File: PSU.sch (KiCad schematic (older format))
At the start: 17 parts, among them P1 CONN_01X02, P2 CONN_01X01, P3 CONN_01X01, P4 CONN_01X01, Q1 BC817-40, U1 78L33

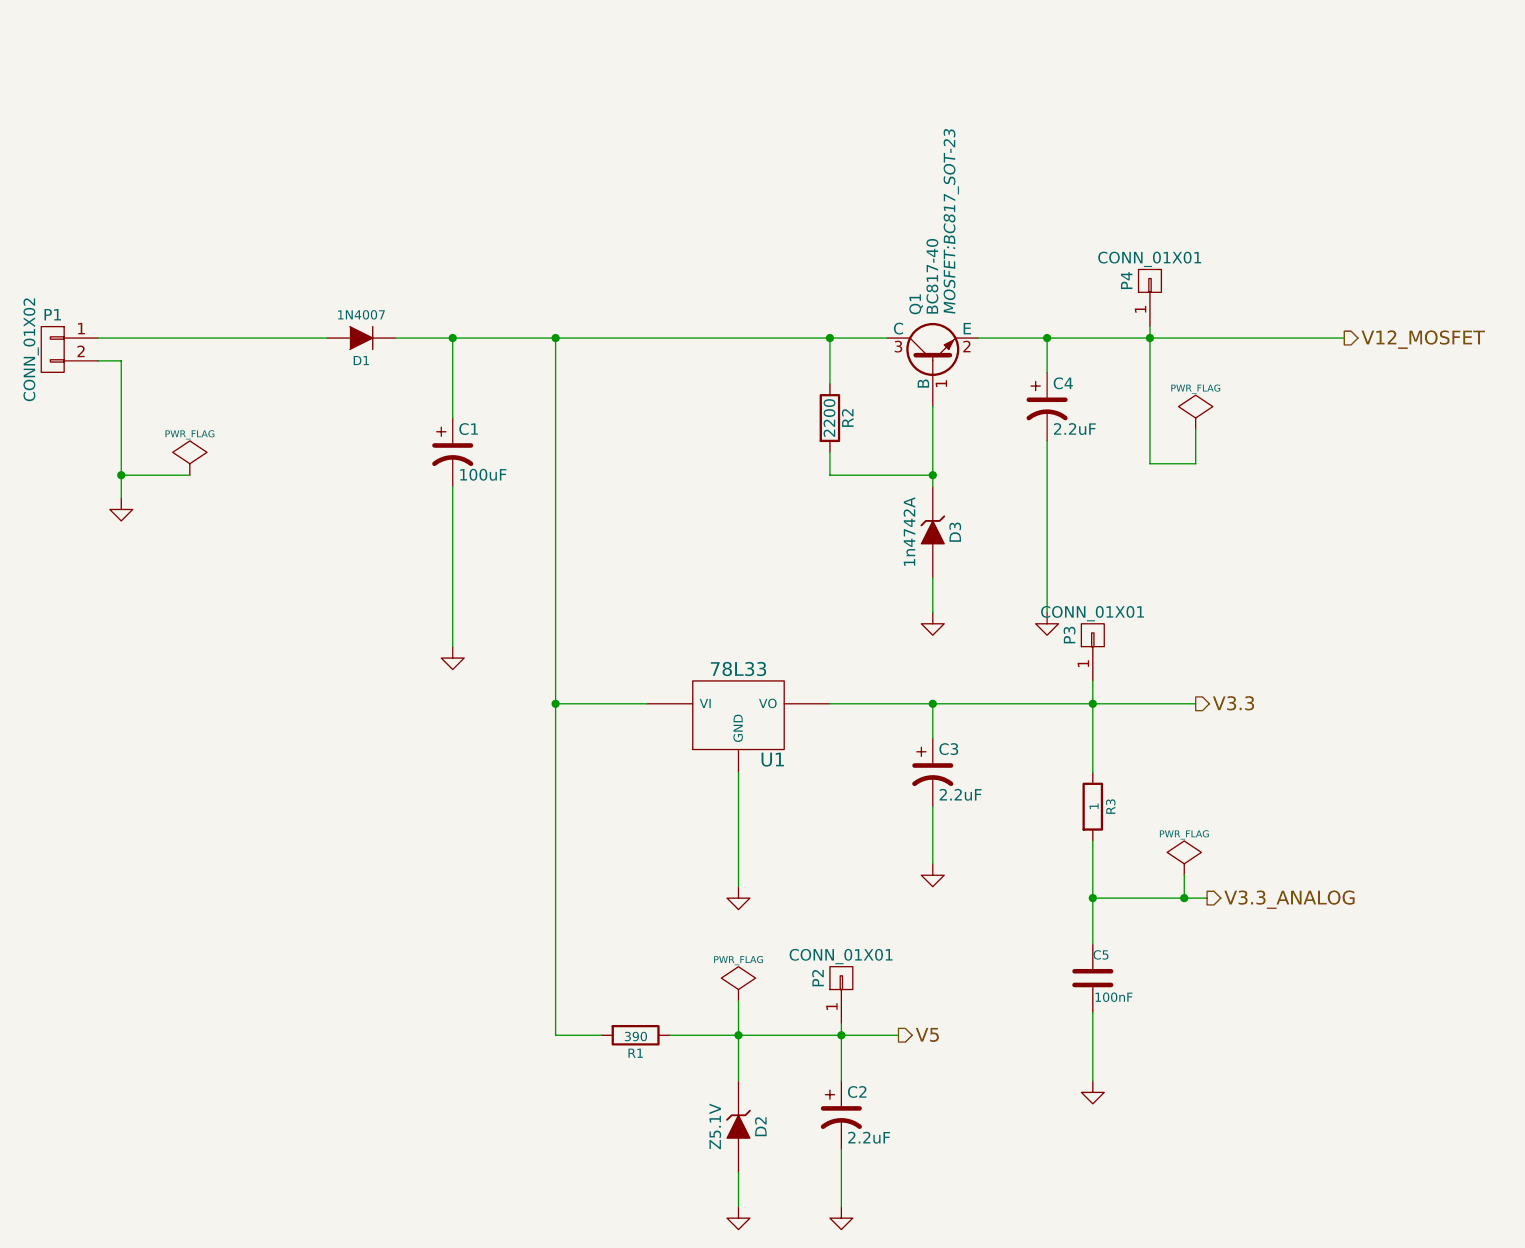
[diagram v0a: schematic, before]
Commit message: agrego librerias de footprint y paso todo al PCB
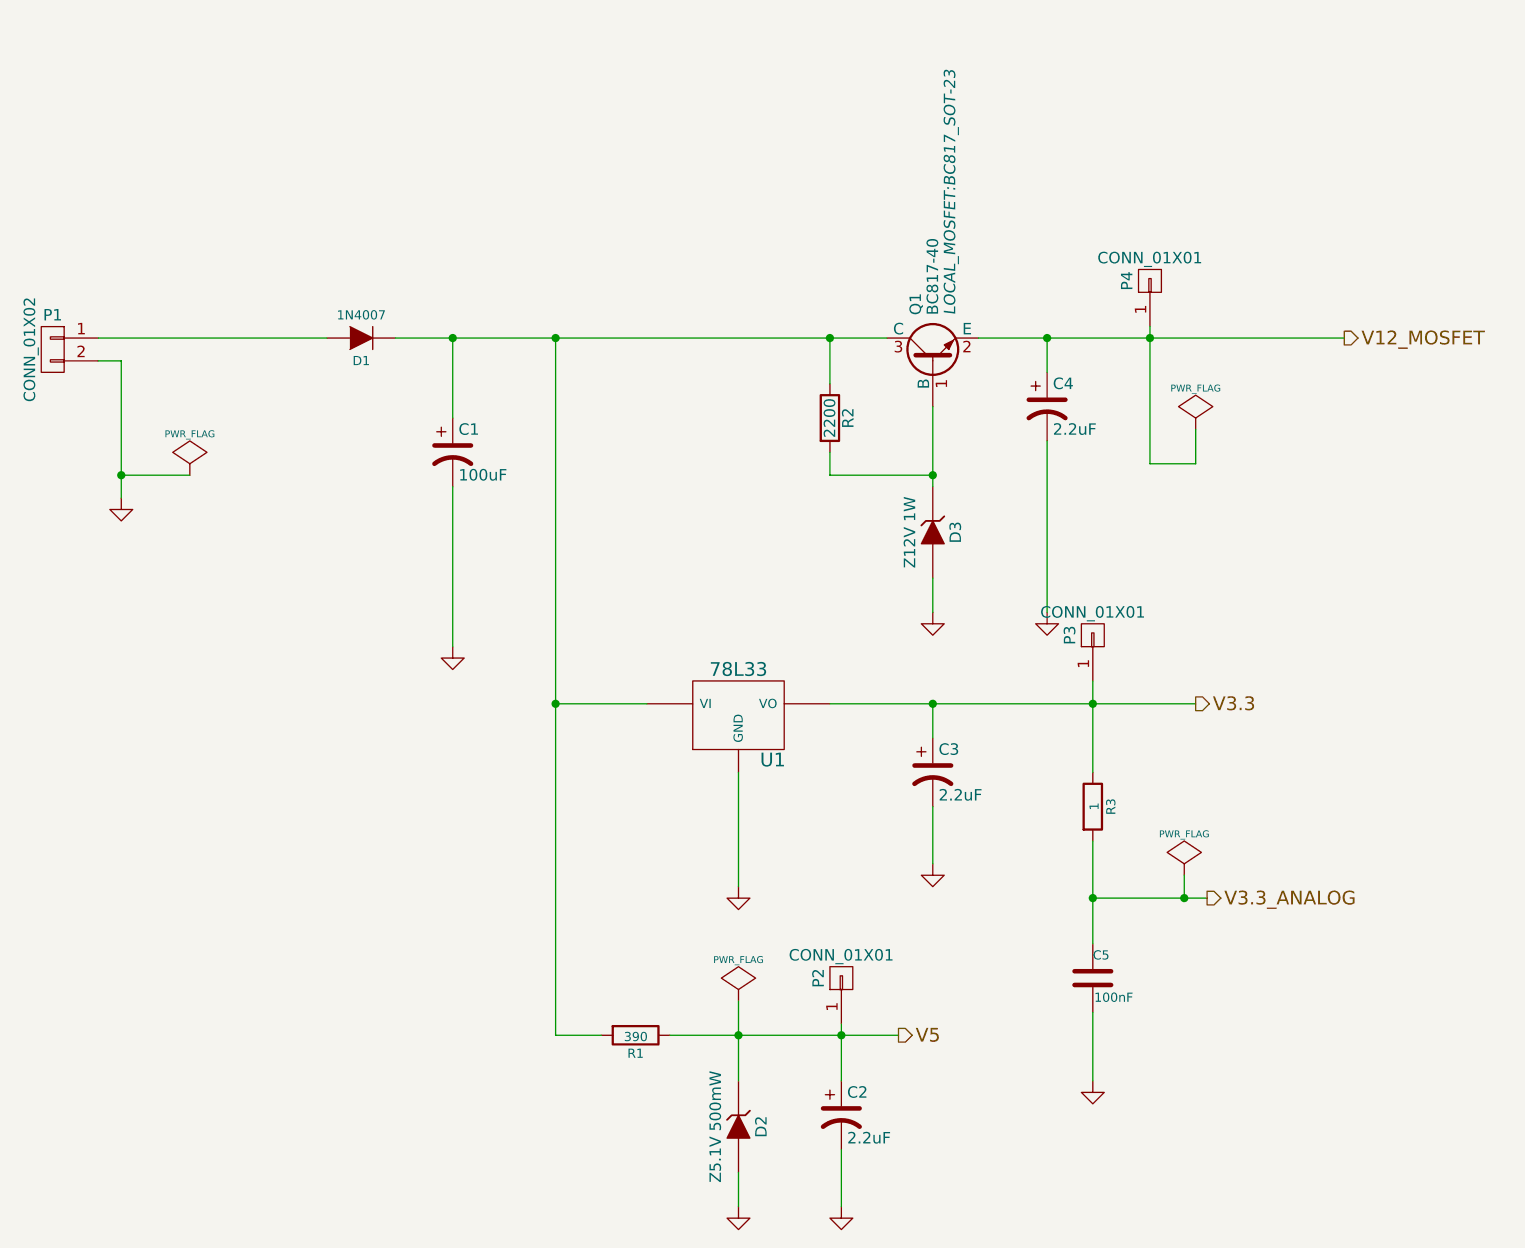
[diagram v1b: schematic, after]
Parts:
- C1: footprint Capacitors_ThroughHole:C_Radial_D10_L13_P5 -> LOCAL_Connectors_Molex:Molex_KK_6410-03
- C2, C3, C4: footprint Capacitors_ThroughHole:C_Radial_D5_L11_P2.5 -> LOCAL_Capacitors_ThroughHole:C_Radial_D5_L11_P2.5
- D1: footprint Diodes_ThroughHole:Diode_DO-41_SOD81_Horizontal_RM10 -> LOCAL_Diode_ThroughHole:Diode_DO-41_SOD81_Horizontal_RM10
- D2: value Z5.1V -> Z5.1V 500mW; footprint Discret:D3 -> LOCAL_Diode_ThroughHole:Diode_DO-41_SOD81_Horizontal_RM10
- D3: value 1n4742A -> Z12V 1W; footprint Discret:D3 -> LOCAL_Diode_ThroughHole:Diode_DO-41_SOD81_Horizontal_RM10
- P2, P3, P4: footprint Pin_Headers:Pin_Header_Straight_1x01 -> LOCAL_Pin_Headers:Pin_Header_Straight_1x01
- Q1: footprint MOSFET:BC817_SOT-23 -> LOCAL_MOSFET:BC817_SOT-23
- U1: footprint TO_SOT_Packages_THT:TO-92_Inline_Wide -> LOCAL_TO_SOT_Packages_THT:TO-92_Inline_Wide
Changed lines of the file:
@@
 F 0 "D1" H 3750 1650 40  0000 C CNN
 F 1 "1N4007" H 3750 1450 40  0000 C CNN
-F 2 "Diodes_ThroughHole:Diode_DO-41_SOD81_Horizontal_RM10" H 3750 1550 60  0001 C CNN
+F 2 "LOCAL_Diode_ThroughHole:Diode_DO-41_SOD81_Horizontal_RM10" H 3750 1550 60  0001 C CNN
 F 3 "~" H 3750 1550 60  0000 C CNN
 	1    3750 1550
@@
 P 6250 2400
 F 0 "D3" H 6250 2500 50  0000 C CNN
-F 1 "1n4742A" H 6250 2300 50  0000 C CNN
-F 2 "Discret:D3" H 6250 2400 60  0001 C CNN
+F 1 "Z12V 1W" H 6250 2300 50  0000 C CNN
+F 2 "LOCAL_Diode_ThroughHole:Diode_DO-41_SOD81_Horizontal_RM10" H 6250 2400 60  0001 C CNN
 F 3 "" H 6250 2400 60  0000 C CNN
 	1    6250 2400
@@
 F 0 "P4" H 7200 1400 50  0000 C CNN
 F 1 "CONN_01X01" V 7300 1300 50  0000 C CNN
-F 2 "Pin_Headers:Pin_Header_Straight_1x01" H 7200 1300 60  0001 C CNN
+F 2 "LOCAL_Pin_Headers:Pin_Header_Straight_1x01" H 7200 1300 60  0001 C CNN
 F 3 "" H 7200 1300 60  0000 C CNN
 	1    7200 1300
@@
 F 0 "P3" H 6950 2950 50  0000 C CNN
 F 1 "CONN_01X01" V 7050 2850 50  0000 C CNN
-F 2 "Pin_Headers:Pin_Header_Straight_1x01" H 6950 2850 60  0001 C CNN
+F 2 "LOCAL_Pin_Headers:Pin_Header_Straight_1x01" H 6950 2850 60  0001 C CNN
 F 3 "" H 6950 2850 60  0000 C CNN
 	1    6950 2850
@@
 F 0 "U1" H 5550 3004 60  0000 C CNN
 F 1 "78L33" H 5400 3400 60  0000 C CNN
-F 2 "TO_SOT_Packages_THT:TO-92_Inline_Wide" H 5400 3200 60  0001 C CNN
+F 2 "LOCAL_TO_SOT_Packages_THT:TO-92_Inline_Wide" H 5400 3200 60  0001 C CNN
 F 3 "" H 5400 3200 60  0000 C CNN
 	1    5400 3200
@@
 F 0 "C1" H 4175 2150 50  0000 L CNN
 F 1 "100uF" H 4175 1950 50  0000 L CNN
-F 2 "Capacitors_ThroughHole:C_Radial_D10_L13_P5" H 4150 2050 60  0001 C CNN
+F 2 "LOCAL_Connectors_Molex:Molex_KK_6410-03" H 4150 2050 60  0001 C CNN
 F 3 "" H 4150 2050 60  0000 C CNN
 	1    4150 2050
@@
 F 0 "C4" H 6775 1950 50  0000 L CNN
 F 1 "2.2uF" H 6775 1750 50  0000 L CNN
-F 2 "Capacitors_ThroughHole:C_Radial_D5_L11_P2.5" H 6750 1850 60  0001 C CNN
+F 2 "LOCAL_Capacitors_ThroughHole:C_Radial_D5_L11_P2.5" H 6750 1850 60  0001 C CNN
 F 3 "" H 6750 1850 60  0000 C CNN
 	1    6750 1850
@@
 F 0 "C3" H 6275 3550 50  0000 L CNN
 F 1 "2.2uF" H 6275 3350 50  0000 L CNN
-F 2 "Capacitors_ThroughHole:C_Radial_D5_L11_P2.5" H 6250 3450 60  0001 C CNN
+F 2 "LOCAL_Capacitors_ThroughHole:C_Radial_D5_L11_P2.5" H 6250 3450 60  0001 C CNN
 F 3 "" H 6250 3450 60  0000 C CNN
 	1    6250 3450
@@
 F 0 "P2" H 5850 4450 50  0000 C CNN
 F 1 "CONN_01X01" V 5950 4350 50  0000 C CNN
-F 2 "Pin_Headers:Pin_Header_Straight_1x01" H 5850 4350 60  0001 C CNN
+F 2 "LOCAL_Pin_Headers:Pin_Header_Straight_1x01" H 5850 4350 60  0001 C CNN
 F 3 "" H 5850 4350 60  0000 C CNN
 	1    5850 4350
@@
 P 5400 5000
 F 0 "D2" H 5400 5100 50  0000 C CNN
-F 1 "Z5.1V" H 5400 4900 50  0000 C CNN
-F 2 "Discret:D3" H 5400 5000 60  0001 C CNN
+F 1 "Z5.1V 500mW" H 5400 4900 50  0000 C CNN
+F 2 "LOCAL_Diode_ThroughHole:Diode_DO-41_SOD81_Horizontal_RM10" H 5400 5000 60  0001 C CNN
 F 3 "" H 5400 5000 60  0000 C CNN
 	1    5400 5000
@@
 F 0 "C2" H 5875 5050 50  0000 L CNN
 F 1 "2.2uF" H 5875 4850 50  0000 L CNN
-F 2 "Capacitors_ThroughHole:C_Radial_D5_L11_P2.5" H 5850 4950 60  0001 C CNN
+F 2 "LOCAL_Capacitors_ThroughHole:C_Radial_D5_L11_P2.5" H 5850 4950 60  0001 C CNN
 F 3 "" H 5850 4950 60  0000 C CNN
 	1    5850 4950
@@
 F 0 "Q1" H 6450 1725 50  0000 L CNN
 F 1 "BC817-40" H 6450 1650 50  0000 L CNN
-F 2 "MOSFET:BC817_SOT-23" H 6450 1575 50  0000 L CIN
+F 2 "LOCAL_MOSFET:BC817_SOT-23" H 6450 1575 50  0000 L CIN
 F 3 "" H 6250 1650 50  0000 L CNN
 	1    6250 1650

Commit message: empiezo a rutear
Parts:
- C1: footprint LOCAL_Connectors_Molex:Molex_KK_6410-03 -> LOCAL_Capacitors_ThroughHole:C_Radial_D10_L20_P5
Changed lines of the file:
@@
 F 0 "C1" H 4175 2150 50  0000 L CNN
 F 1 "100uF" H 4175 1950 50  0000 L CNN
-F 2 "LOCAL_Connectors_Molex:Molex_KK_6410-03" H 4150 2050 60  0001 C CNN
+F 2 "LOCAL_Capacitors_ThroughHole:C_Radial_D10_L20_P5" H 4150 2050 60  0001 C CNN
 F 3 "" H 4150 2050 60  0000 C CNN
 	1    4150 2050

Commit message: mas routeado casi terminado
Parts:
- R1: footprint Resistors_SMD:R_0805_HandSoldering -> Resistors_ThroughHole:Resistor_Horizontal_RM7mm
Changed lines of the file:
@@
 F 0 "R1" V 5030 4600 40  0000 C CNN
 F 1 "390" V 4957 4601 40  0000 C CNN
-F 2 "Resistors_SMD:R_0805_HandSoldering" V 4880 4600 30  0001 C CNN
+F 2 "Resistors_ThroughHole:Resistor_Horizontal_RM7mm" V 4880 4600 30  0001 C CNN
 F 3 "~" H 4950 4600 30  0000 C CNN
 	1    4950 4600

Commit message: todo ruteado y pasa DRC
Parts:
- removed P2: CONN_01X01, LOCAL_Pin_Headers:Pin_Header_Straight_1x01, symbol CONN_01X01
- D3: footprint LOCAL_Diode_ThroughHole:Diode_DO-41_SOD81_Horizontal_RM10 -> Diodes_SMD:MELF_Handsoldering
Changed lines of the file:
@@
 F 0 "D3" H 6250 2500 50  0000 C CNN
 F 1 "Z12V 1W" H 6250 2300 50  0000 C CNN
-F 2 "LOCAL_Diode_ThroughHole:Diode_DO-41_SOD81_Horizontal_RM10" H 6250 2400 60  0001 C CNN
+F 2 "Diodes_SMD:MELF_Handsoldering" H 6250 2400 60  0001 C CNN
 F 3 "" H 6250 2400 60  0000 C CNN
 	1    6250 2400
@@
 	6950 4000 7450 4000
 $Comp
-L CONN_01X01 P2
-U 1 1 56FC5C09
-P 5850 4350
-F 0 "P2" H 5850 4450 50  0000 C CNN
-F 1 "CONN_01X01" V 5950 4350 50  0000 C CNN
-F 2 "LOCAL_Pin_Headers:Pin_Header_Straight_1x01" H 5850 4350 60  0001 C CNN
-F 3 "" H 5850 4350 60  0000 C CNN
-	1    5850 4350
-	0    -1   -1   0
-$EndComp
-$Comp
 L ZENER D2
 U 1 1 56FC5C0A
@@
 Wire Wire Line
 	5400 4450 5400 4800
-Wire Wire Line
-	5850 4550 5850 4800
 $Comp
 L GND #PWR012
@@
 	0    -1   -1   0
 $EndComp
+Wire Wire Line
+	5850 4800 5850 4600
 $EndSCHEMATC
